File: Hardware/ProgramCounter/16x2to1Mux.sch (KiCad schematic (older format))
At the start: 8 parts

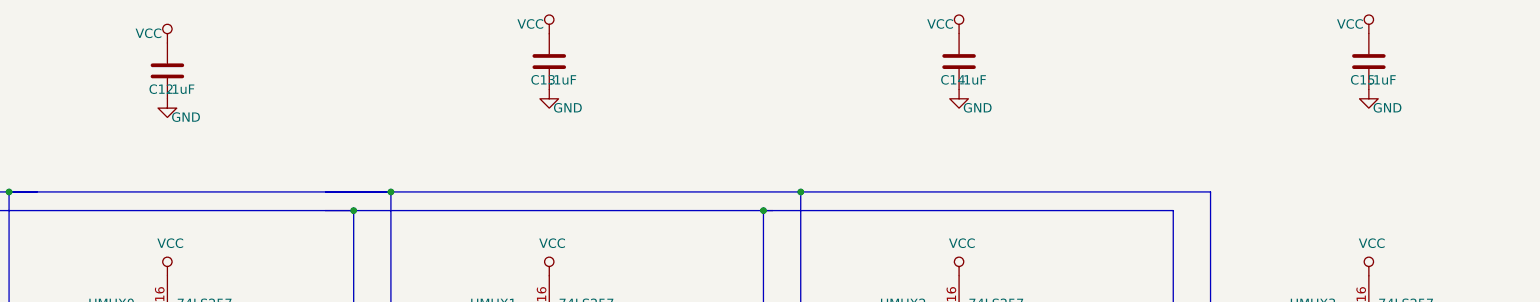
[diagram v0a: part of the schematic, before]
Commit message: PC PCB Progress
Mostly done with schematic for the Program Counter. I'll order parts soon and start on the PCB design next. It'll be my first four layer board!

Based on what I've seen so far, CMOS seems to be more prevalent than TTL, so I'll make this computer out of CMOS.
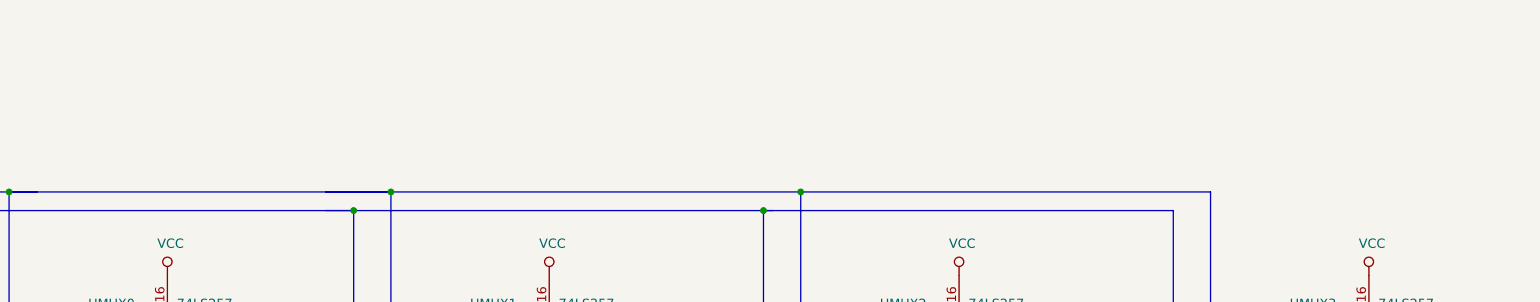
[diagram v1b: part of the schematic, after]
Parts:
- removed C12, C13, C14, C15: .1uF, symbol Device:C
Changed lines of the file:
@@
 Wire Notes Line
 	5200 6250 5400 6150
-$Comp
-L power:VCC #PWR?
-U 1 1 62A1C004
-P 2300 900
-AR Path="/62A1C004" Ref="#PWR?"  Part="1"
-AR Path="/629C34E6/62A1C004" Ref="#PWR0162"  Part="1"
-F 0 "#PWR0162" H 2300 750 50  0001 C CNN
-F 1 "VCC" H 2200 950 50  0000 C CNN
-F 2 "" H 2300 900 50  0001 C CNN
-F 3 "" H 2300 900 50  0001 C CNN
-	1    2300 900
-	1    0    0    -1
-$EndComp
-$Comp
-L Device:C C?
-U 1 1 62A1C00A
-P 2300 1050
-AR Path="/62A1C00A" Ref="C?"  Part="1"
-AR Path="/629C34E6/62A1C00A" Ref="C12"  Part="1"
-F 0 "C12" H 2200 950 50  0000 L CNN
-F 1 ".1uF" H 2300 950 50  0000 L CNN
-F 2 "" H 2338 900 50  0001 C CNN
-F 3 "~" H 2300 1050 50  0001 C CNN
-	1    2300 1050
-	1    0    0    -1
-$EndComp
-$Comp
-L power:GND #PWR?
-U 1 1 62A1C010
-P 2300 1200
-AR Path="/62A1C010" Ref="#PWR?"  Part="1"
-AR Path="/629C34E6/62A1C010" Ref="#PWR0163"  Part="1"
-F 0 "#PWR0163" H 2300 950 50  0001 C CNN
-F 1 "GND" H 2400 1100 50  0000 C CNN
-F 2 "" H 2300 1200 50  0001 C CNN
-F 3 "" H 2300 1200 50  0001 C CNN
-	1    2300 1200
-	1    0    0    -1
-$EndComp
-$Comp
-L power:VCC #PWR?
-U 1 1 62A1F903
-P 4350 850
-AR Path="/62A1F903" Ref="#PWR?"  Part="1"
-AR Path="/629C34E6/62A1F903" Ref="#PWR0164"  Part="1"
-F 0 "#PWR0164" H 4350 700 50  0001 C CNN
-F 1 "VCC" H 4250 900 50  0000 C CNN
-F 2 "" H 4350 850 50  0001 C CNN
-F 3 "" H 4350 850 50  0001 C CNN
-	1    4350 850
-	1    0    0    -1
-$EndComp
-$Comp
-L Device:C C?
-U 1 1 62A1F909
-P 4350 1000
-AR Path="/62A1F909" Ref="C?"  Part="1"
-AR Path="/629C34E6/62A1F909" Ref="C13"  Part="1"
-F 0 "C13" H 4250 900 50  0000 L CNN
-F 1 ".1uF" H 4350 900 50  0000 L CNN
-F 2 "" H 4388 850 50  0001 C CNN
-F 3 "~" H 4350 1000 50  0001 C CNN
-	1    4350 1000
-	1    0    0    -1
-$EndComp
-$Comp
-L power:GND #PWR?
-U 1 1 62A1F90F
-P 4350 1150
-AR Path="/62A1F90F" Ref="#PWR?"  Part="1"
-AR Path="/629C34E6/62A1F90F" Ref="#PWR0165"  Part="1"
-F 0 "#PWR0165" H 4350 900 50  0001 C CNN
-F 1 "GND" H 4450 1050 50  0000 C CNN
-F 2 "" H 4350 1150 50  0001 C CNN
-F 3 "" H 4350 1150 50  0001 C CNN
-	1    4350 1150
-	1    0    0    -1
-$EndComp
-$Comp
-L power:VCC #PWR?
-U 1 1 62A229D7
-P 6550 850
-AR Path="/62A229D7" Ref="#PWR?"  Part="1"
-AR Path="/629C34E6/62A229D7" Ref="#PWR0166"  Part="1"
-F 0 "#PWR0166" H 6550 700 50  0001 C CNN
-F 1 "VCC" H 6450 900 50  0000 C CNN
-F 2 "" H 6550 850 50  0001 C CNN
-F 3 "" H 6550 850 50  0001 C CNN
-	1    6550 850
-	1    0    0    -1
-$EndComp
-$Comp
-L Device:C C?
-U 1 1 62A229DD
-P 6550 1000
-AR Path="/62A229DD" Ref="C?"  Part="1"
-AR Path="/629C34E6/62A229DD" Ref="C14"  Part="1"
-F 0 "C14" H 6450 900 50  0000 L CNN
-F 1 ".1uF" H 6550 900 50  0000 L CNN
-F 2 "" H 6588 850 50  0001 C CNN
-F 3 "~" H 6550 1000 50  0001 C CNN
-	1    6550 1000
-	1    0    0    -1
-$EndComp
-$Comp
-L power:GND #PWR?
-U 1 1 62A229E3
-P 6550 1150
-AR Path="/62A229E3" Ref="#PWR?"  Part="1"
-AR Path="/629C34E6/62A229E3" Ref="#PWR0167"  Part="1"
-F 0 "#PWR0167" H 6550 900 50  0001 C CNN
-F 1 "GND" H 6650 1050 50  0000 C CNN
-F 2 "" H 6550 1150 50  0001 C CNN
-F 3 "" H 6550 1150 50  0001 C CNN
-	1    6550 1150
-	1    0    0    -1
-$EndComp
-$Comp
-L power:VCC #PWR?
-U 1 1 62A25952
-P 8750 850
-AR Path="/62A25952" Ref="#PWR?"  Part="1"
-AR Path="/629C34E6/62A25952" Ref="#PWR0168"  Part="1"
-F 0 "#PWR0168" H 8750 700 50  0001 C CNN
-F 1 "VCC" H 8650 900 50  0000 C CNN
-F 2 "" H 8750 850 50  0001 C CNN
-F 3 "" H 8750 850 50  0001 C CNN
-	1    8750 850
-	1    0    0    -1
-$EndComp
-$Comp
-L Device:C C?
-U 1 1 62A25958
-P 8750 1000
-AR Path="/62A25958" Ref="C?"  Part="1"
-AR Path="/629C34E6/62A25958" Ref="C15"  Part="1"
-F 0 "C15" H 8650 900 50  0000 L CNN
-F 1 ".1uF" H 8750 900 50  0000 L CNN
-F 2 "" H 8788 850 50  0001 C CNN
-F 3 "~" H 8750 1000 50  0001 C CNN
-	1    8750 1000
-	1    0    0    -1
-$EndComp
-$Comp
-L power:GND #PWR?
-U 1 1 62A2595E
-P 8750 1150
-AR Path="/62A2595E" Ref="#PWR?"  Part="1"
-AR Path="/629C34E6/62A2595E" Ref="#PWR0169"  Part="1"
-F 0 "#PWR0169" H 8750 900 50  0001 C CNN
-F 1 "GND" H 8850 1050 50  0000 C CNN
-F 2 "" H 8750 1150 50  0001 C CNN
-F 3 "" H 8750 1150 50  0001 C CNN
-	1    8750 1150
-	1    0    0    -1
-$EndComp
 Wire Bus Line
 	3100 2550 3100 4700

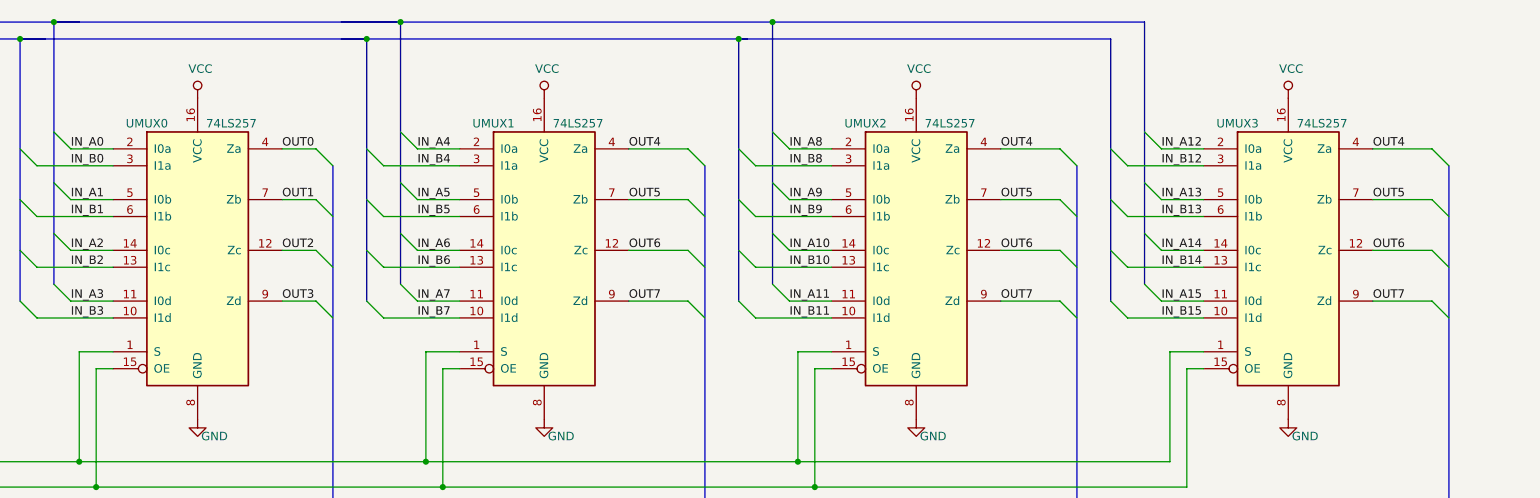
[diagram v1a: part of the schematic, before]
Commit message: PC Schematic
Mostly finished Program Counter schematic. I'm basing the hardware largely off of TI's new HCS family of SN74HCS chips.
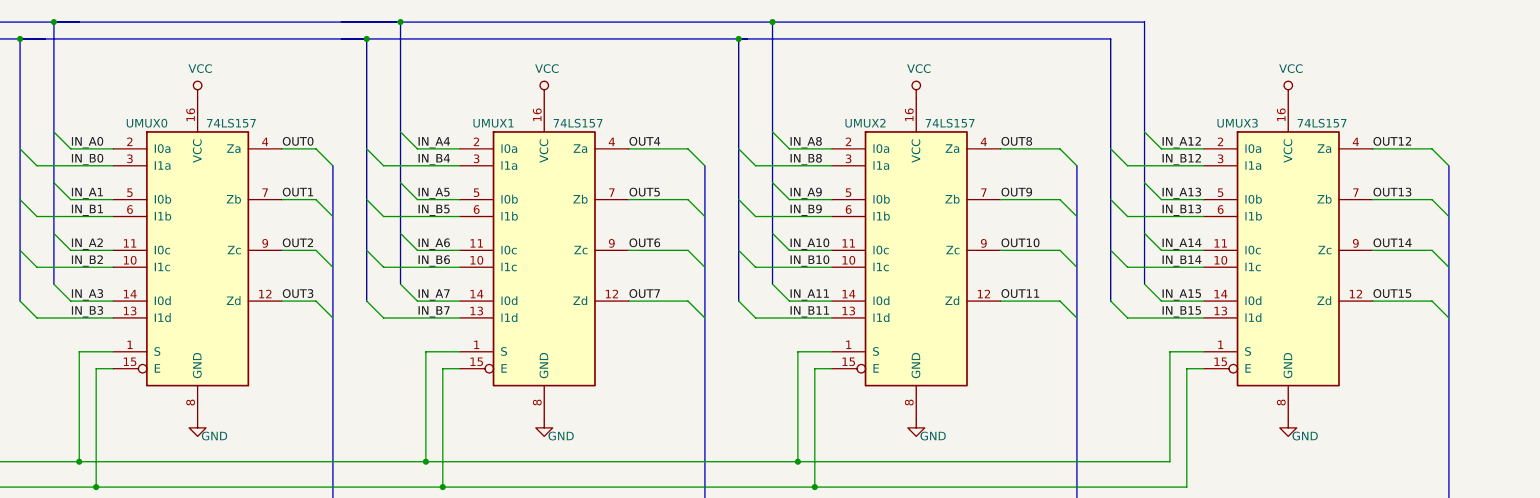
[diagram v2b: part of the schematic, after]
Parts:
- removed UMUX0, UMUX1, UMUX2, UMUX3: 74LS257, Package_SO:TSSOP-16_4.4x5mm_P0.65mm, symbol 74xx:74LS257
- added UMUX0, UMUX1, UMUX2, UMUX3: 74LS157, aFootprint:R-PDSO-G16, symbol 74xx:74LS157
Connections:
- net GND: now also UMUX0.8 (GND), UMUX1.8 (GND), UMUX2.8 (GND), UMUX3.8 (GND)
- net IN_A0: now also UMUX0.2 (I0a)
- net IN_A1: now also UMUX0.5 (I0b)
- net IN_A10: now also UMUX2.11 (I0c)
- net IN_A11: now also UMUX2.14 (I0d)
- net IN_A12: now also UMUX3.2 (I0a)
- net IN_A13: now also UMUX3.5 (I0b)
- net IN_A14: now also UMUX3.11 (I0c)
- net IN_A15: now also UMUX3.14 (I0d)
- net IN_A2: now also UMUX0.11 (I0c)
- net IN_A3: now also UMUX0.14 (I0d)
- net IN_A4: now also UMUX1.2 (I0a)
- net IN_A5: now also UMUX1.5 (I0b)
- net IN_A6: now also UMUX1.11 (I0c)
- net IN_A7: now also UMUX1.14 (I0d)
- net IN_A8: now also UMUX2.2 (I0a)
- net IN_A9: now also UMUX2.5 (I0b)
- net IN_B0: now also UMUX0.3 (I1a)
- net IN_B1: now also UMUX0.6 (I1b)
- net IN_B10: now also UMUX2.10 (I1c)
- net IN_B11: now also UMUX2.13 (I1d)
- net IN_B12: now also UMUX3.3 (I1a)
- net IN_B13: now also UMUX3.6 (I1b)
- net IN_B14: now also UMUX3.10 (I1c)
- net IN_B15: now also UMUX3.13 (I1d)
- net IN_B2: now also UMUX0.10 (I1c)
- net IN_B3: now also UMUX0.13 (I1d)
- net IN_B4: now also UMUX1.3 (I1a)
- net IN_B5: now also UMUX1.6 (I1b)
- net IN_B6: now also UMUX1.10 (I1c)
- net IN_B7: now also UMUX1.13 (I1d)
- net IN_B8: now also UMUX2.3 (I1a)
- net IN_B9: now also UMUX2.6 (I1b)
- net OUT0: now also UMUX0.4 (Za)
- net OUT1: now also UMUX0.7 (Zb)
- net OUT2: now also UMUX0.9 (Zc)
- net OUT3: now also UMUX0.12 (Zd)
- net OUT4: now also UMUX1.4 (Za)
- net OUT5: now also UMUX1.7 (Zb)
- net OUT6: now also UMUX1.9 (Zc)
- net OUT7: now also UMUX1.12 (Zd)
- net SELECT: now also UMUX0.1 (S), UMUX1.1 (S), UMUX2.1 (S), UMUX3.1 (S)
- net VCC: now also UMUX0.16 (VCC), UMUX1.16 (VCC), UMUX2.16 (VCC), UMUX3.16 (VCC)
- net ~OE: now also UMUX0.15 (E), UMUX1.15 (E), UMUX2.15 (E), UMUX3.15 (E)
- new net OUT10: UMUX2.9 (Zc)
- new net OUT11: UMUX2.12 (Zd)
- new net OUT12: UMUX3.4 (Za)
- new net OUT13: UMUX3.7 (Zb)
- new net OUT14: UMUX3.9 (Zc)
- new net OUT15: UMUX3.12 (Zd)
- new net OUT8: UMUX2.4 (Za)
- new net OUT9: UMUX2.7 (Zb)
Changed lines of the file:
@@
 $EndDescr
-$Comp
-L 74xx:74LS257 UNEXTPC?
-U 1 1 629C7F9D
-P 2300 3050
-AR Path="/629C7F9D" Ref="UNEXTPC?"  Part="1"
-AR Path="/629C34E6/629C7F9D" Ref="UMUX0"  Part="1"
-F 0 "UMUX0" H 2000 3800 50  0000 C CNN
-F 1 "74LS257" H 2500 3800 50  0000 C CNN
-F 2 "Package_SO:TSSOP-16_4.4x5mm_P0.65mm" H 2300 3050 50  0001 C CNN
-F 3 "http://www.ti.com/lit/gpn/sn74LS257" H 2300 3050 50  0001 C CNN
-	1    2300 3050
-	1    0    0    -1
-$EndComp
 $Comp
 L power:VCC #PWR?
@@
 	1    0    0    -1
 $EndComp
-$Comp
-L 74xx:74LS257 UMUX?
-U 1 1 62A15465
-P 4350 3050
-AR Path="/62A15465" Ref="UMUX?"  Part="1"
-AR Path="/629C34E6/62A15465" Ref="UMUX1"  Part="1"
-F 0 "UMUX1" H 4050 3800 50  0000 C CNN
-F 1 "74LS257" H 4550 3800 50  0000 C CNN
-F 2 "Package_SO:TSSOP-16_4.4x5mm_P0.65mm" H 4350 3050 50  0001 C CNN
-F 3 "http://www.ti.com/lit/gpn/sn74LS257" H 4350 3050 50  0001 C CNN
-	1    4350 3050
-	1    0    0    -1
-$EndComp
 Connection ~ 3300 1800
 Connection ~ 3500 1700
@@
 	7400 2450 7500 2550
 Text Label 7050 3350 0    50   ~ 0
-OUT7
+OUT11
 Text Label 7050 3050 0    50   ~ 0
-OUT6
+OUT10
 Text Label 7050 2750 0    50   ~ 0
-OUT5
+OUT9
 Wire Wire Line
 	7050 3050 7400 3050
@@
 	7050 2450 7400 2450
 Text Label 7050 2450 0    50   ~ 0
-OUT4
+OUT8
 Wire Wire Line
 	7050 3350 7400 3350
@@
 	1    0    0    -1
 $EndComp
-$Comp
-L 74xx:74LS257 UMUX?
-U 1 1 62A3D5E6
-P 6550 3050
-AR Path="/62A3D5E6" Ref="UMUX?"  Part="1"
-AR Path="/629C34E6/62A3D5E6" Ref="UMUX2"  Part="1"
-F 0 "UMUX2" H 6250 3800 50  0000 C CNN
-F 1 "74LS257" H 6750 3800 50  0000 C CNN
-F 2 "Package_SO:TSSOP-16_4.4x5mm_P0.65mm" H 6550 3050 50  0001 C CNN
-F 3 "http://www.ti.com/lit/gpn/sn74LS257" H 6550 3050 50  0001 C CNN
-	1    6550 3050
-	1    0    0    -1
-$EndComp
 Entry Wire Line
 	9600 3350 9700 3450
@@
 	9600 2450 9700 2550
 Text Label 9250 3350 0    50   ~ 0
-OUT7
+OUT15
 Text Label 9250 3050 0    50   ~ 0
-OUT6
+OUT14
 Text Label 9250 2750 0    50   ~ 0
-OUT5
+OUT13
 Wire Wire Line
 	9250 3050 9600 3050
@@
 	9250 2450 9600 2450
 Text Label 9250 2450 0    50   ~ 0
-OUT4
+OUT12
 Wire Wire Line
 	9250 3350 9600 3350
@@
 	1    0    0    -1
 $EndComp
-$Comp
-L 74xx:74LS257 UMUX?
-U 1 1 62A4288C
-P 8750 3050
-AR Path="/62A4288C" Ref="UMUX?"  Part="1"
-AR Path="/629C34E6/62A4288C" Ref="UMUX3"  Part="1"
-F 0 "UMUX3" H 8450 3800 50  0000 C CNN
-F 1 "74LS257" H 8950 3800 50  0000 C CNN
-F 2 "Package_SO:TSSOP-16_4.4x5mm_P0.65mm" H 8750 3050 50  0001 C CNN
-F 3 "http://www.ti.com/lit/gpn/sn74LS257" H 8750 3050 50  0001 C CNN
-	1    8750 3050
-	1    0    0    -1
-$EndComp
 Wire Wire Line
 	8050 4300 5850 4300
@@
 Wire Notes Line
 	5200 6250 5400 6150
+$Comp
+L 74xx:74LS157 UMUX0
+U 1 1 626E121B
+P 2300 3050
+F 0 "UMUX0" H 2000 3800 50  0000 C CNN
+F 1 "74LS157" H 2500 3800 50  0000 C CNN
+F 2 "aFootprint:R-PDSO-G16" H 2300 3050 50  0001 C CNN
+F 3 "http://www.ti.com/lit/gpn/sn74LS157" H 2300 3050 50  0001 C CNN
+	1    2300 3050
+	1    0    0    -1
+$EndComp
+$Comp
+L 74xx:74LS157 UMUX1
+U 1 1 626E4097
+P 4350 3050
+F 0 "UMUX1" H 4050 3800 50  0000 C CNN
+F 1 "74LS157" H 4550 3800 50  0000 C CNN
+F 2 "aFootprint:R-PDSO-G16" H 4350 3050 50  0001 C CNN
+F 3 "http://www.ti.com/lit/gpn/sn74LS157" H 4350 3050 50  0001 C CNN
+	1    4350 3050
+	1    0    0    -1
+$EndComp
+$Comp
+L 74xx:74LS157 UMUX2
+U 1 1 626E53F5
+P 6550 3050
+F 0 "UMUX2" H 6250 3800 50  0000 C CNN
+F 1 "74LS157" H 6750 3800 50  0000 C CNN
+F 2 "aFootprint:R-PDSO-G16" H 6550 3050 50  0001 C CNN
+F 3 "http://www.ti.com/lit/gpn/sn74LS157" H 6550 3050 50  0001 C CNN
+	1    6550 3050
+	1    0    0    -1
+$EndComp
+$Comp
+L 74xx:74LS157 UMUX3
+U 1 1 626E5F78
+P 8750 3050
+F 0 "UMUX3" H 8450 3800 50  0000 C CNN
+F 1 "74LS157" H 8950 3800 50  0000 C CNN
+F 2 "aFootprint:R-PDSO-G16" H 8750 3050 50  0001 C CNN
+F 3 "http://www.ti.com/lit/gpn/sn74LS157" H 8750 3050 50  0001 C CNN
+	1    8750 3050
+	1    0    0    -1
+$EndComp
 Wire Bus Line
 	3100 2550 3100 4700

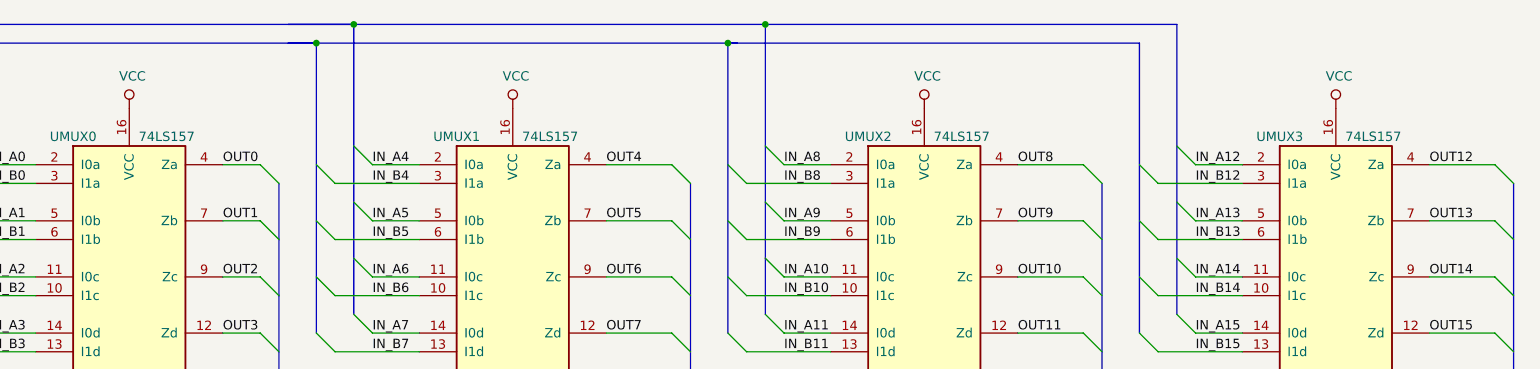
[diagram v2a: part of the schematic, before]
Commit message: PC Board
Mostly done. Going to move top half down.
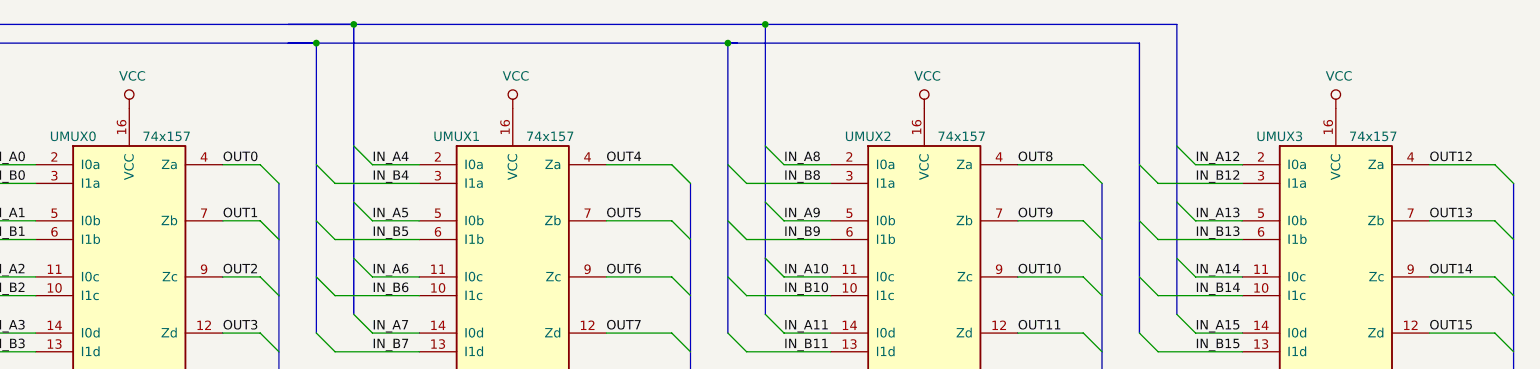
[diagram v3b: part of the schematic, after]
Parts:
- UMUX0, UMUX1, UMUX2, UMUX3: value 74LS157 -> 74x157
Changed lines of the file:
@@
 	5200 6250 5400 6150
-$Comp
-L 74xx:74LS157 UMUX0
-U 1 1 626E121B
-P 2300 3050
-F 0 "UMUX0" H 2000 3800 50  0000 C CNN
-F 1 "74LS157" H 2500 3800 50  0000 C CNN
-F 2 "aFootprint:R-PDSO-G16" H 2300 3050 50  0001 C CNN
-F 3 "http://www.ti.com/lit/gpn/sn74LS157" H 2300 3050 50  0001 C CNN
-	1    2300 3050
-	1    0    0    -1
-$EndComp
 $Comp
 L 74xx:74LS157 UMUX1
@@
 P 4350 3050
 F 0 "UMUX1" H 4050 3800 50  0000 C CNN
-F 1 "74LS157" H 4550 3800 50  0000 C CNN
+F 1 "74x157" H 4550 3800 50  0000 C CNN
 F 2 "aFootprint:R-PDSO-G16" H 4350 3050 50  0001 C CNN
 F 3 "http://www.ti.com/lit/gpn/sn74LS157" H 4350 3050 50  0001 C CNN
@@
 P 6550 3050
 F 0 "UMUX2" H 6250 3800 50  0000 C CNN
-F 1 "74LS157" H 6750 3800 50  0000 C CNN
+F 1 "74x157" H 6750 3800 50  0000 C CNN
 F 2 "aFootprint:R-PDSO-G16" H 6550 3050 50  0001 C CNN
 F 3 "http://www.ti.com/lit/gpn/sn74LS157" H 6550 3050 50  0001 C CNN
@@
 P 8750 3050
 F 0 "UMUX3" H 8450 3800 50  0000 C CNN
-F 1 "74LS157" H 8950 3800 50  0000 C CNN
+F 1 "74x157" H 8950 3800 50  0000 C CNN
 F 2 "aFootprint:R-PDSO-G16" H 8750 3050 50  0001 C CNN
 F 3 "http://www.ti.com/lit/gpn/sn74LS157" H 8750 3050 50  0001 C CNN
@@
 	1    0    0    -1
 $EndComp
+$Comp
+L 74xx:74LS157 UMUX0
+U 1 1 626E121B
+P 2300 3050
+F 0 "UMUX0" H 2000 3800 50  0000 C CNN
+F 1 "74x157" H 2500 3800 50  0000 C CNN
+F 2 "aFootprint:R-PDSO-G16" H 2300 3050 50  0001 C CNN
+F 3 "http://www.ti.com/lit/gpn/sn74LS157" H 2300 3050 50  0001 C CNN
+	1    2300 3050
+	1    0    0    -1
+$EndComp
+Wire Bus Line
+	7900 1700 7900 3250
+Wire Bus Line
+	7700 1800 7700 3350
+Wire Bus Line
+	9700 2550 9700 4700
+Wire Bus Line
+	5700 1700 5700 3250
+Wire Bus Line
+	5500 1800 5500 3350
+Wire Bus Line
+	7500 2550 7500 4700
+Wire Bus Line
+	3500 1700 3500 3250
+Wire Bus Line
+	3300 1800 3300 3350
+Wire Bus Line
+	5300 2550 5300 4700
 Wire Bus Line
 	3100 2550 3100 4700
@@
 Wire Bus Line
 	1450 1700 1450 3250
-Wire Bus Line
-	5300 2550 5300 4700
-Wire Bus Line
-	3300 1800 3300 3350
-Wire Bus Line
-	3500 1700 3500 3250
-Wire Bus Line
-	7500 2550 7500 4700
-Wire Bus Line
-	5500 1800 5500 3350
-Wire Bus Line
-	5700 1700 5700 3250
-Wire Bus Line
-	9700 2550 9700 4700
-Wire Bus Line
-	7700 1800 7700 3350
-Wire Bus Line
-	7900 1700 7900 3250
 $EndSCHEMATC
